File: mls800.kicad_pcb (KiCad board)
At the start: 2 copper layers, 293.4 x 80.5 mm, 106 parts, among them CON1 BARREL_JACK, IC1 6N137, J1 USB, J10 NSJ8HC, J11 NRJ4HF-1, J2 NRJ4HF-1, J3 NSJ8HC, J4 NSJ8HC, J5 NSJ8HC, J6 NSJ8HC, J7 NSJ8HC, J8 NSJ8HC, J9 NSJ8HC, P1 CONN_02X03, P2 DIN_5, P3 DIN_5, P4 CONN_02X03, P5 CONN_02X03, SW10 SW_TACT_LED, SW11 SW_TACT_LED, SW12 SW_PUSH_RIGHT_ANGLE, SW2 SW_TACT_LED, SW3 SW_TACT_LED, SW4 SW_TACT_LED, SW5 SW_TACT_LED, SW6 SW_TACT_LED, SW7 SW_TACT_LED, SW8 SW_TACT_LED, SW9 SW_TACT_LED, U1 LM340MP-5.0/NOPB, U2 ATmega32U4-AU, U3 24LC256, U4 MCP23017, U5 AS1115, U6 ULN2803A, U7 ULN2803A, U8 LM340MP-5.0/NOPB, X1 16Mhz

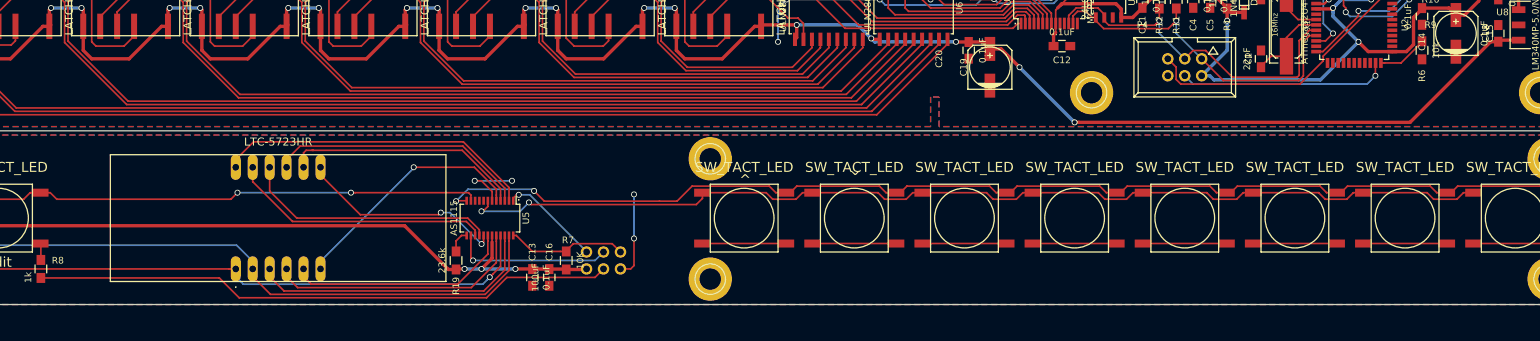
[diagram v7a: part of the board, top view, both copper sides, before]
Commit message: Fixed front panel capacitor footprint
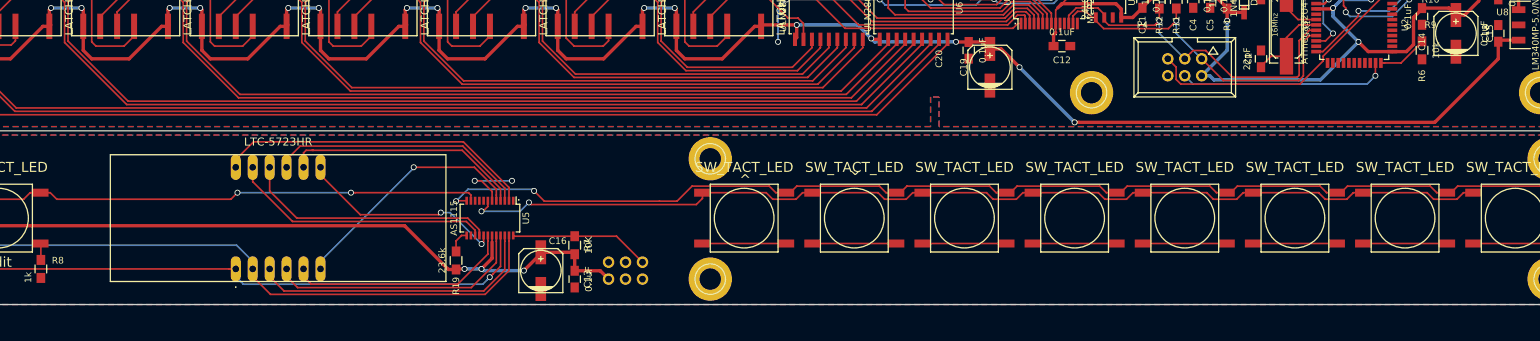
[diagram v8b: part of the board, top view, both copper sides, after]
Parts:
- C16: footprint Capacitors_SMD:C_0805_HandSoldering -> Capacitors_SMD:c_elec_6.3x7.7
- moved C13 6.36 mm to (171.4, 121.9)
- moved P5 3.64 mm to (179.1, 120.7)
- moved R7 2.62 mm to (171.4, 116.8)
- moved C16 1.63 mm to (166.4, 120.7), turned to 90 degrees
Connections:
- CON1 pad 3: (no net) -> Net-(CON1-Pad3)
- IC1 pad 7: (no net) -> Net-(IC1-Pad7)
- J11 pad 2: (no net) -> Net-(J11-Pad2)
- J2 pad 2: (no net) -> Net-(J2-Pad2)
- P2 pad 1: (no net) -> Net-(P2-Pad1)
- P2 pad 3: (no net) -> Net-(P2-Pad3)
- P2 pad 5: (no net) -> Net-(P2-Pad5)
- P3 pad 1: (no net) -> Net-(P3-Pad1)
- P3 pad 5: (no net) -> Net-(P3-Pad5)
- SW2 pad 4: /Front panel/SEGA -> /Front panel/SEGDP
- SW3 pad 4: /Front panel/SEGB -> /Front panel/SEGA
- SW4 pad 4: /Front panel/SEGC -> /Front panel/SEGB
- SW5 pad 4: /Front panel/SEGD -> /Front panel/SEGC
- SW6 pad 4: /Front panel/SEGE -> /Front panel/SEGD
- SW7 pad 4: /Front panel/SEGF -> /Front panel/SEGE
- SW8 pad 4: /Front panel/SEGG -> /Front panel/SEGF
- SW9 pad 4: /Front panel/SEGDP -> /Front panel/SEGDG
- U2 pad 12: (no net) -> Net-(U2-Pad12)
- U2 pad 21: (no net) -> Net-(U2-Pad21)
- U2 pad 24: (no net) -> Net-(U2-Pad24)
- U2 pad 25: (no net) -> Net-(U2-Pad25)
- U2 pad 26: (no net) -> Net-(U2-Pad26)
- U2 pad 27: (no net) -> Net-(U2-Pad27)
- U2 pad 28: (no net) -> Net-(U2-Pad28)
- U2 pad 29: (no net) -> Net-(U2-Pad29)
- U2 pad 30: (no net) -> Net-(U2-Pad30)
- U2 pad 31: (no net) -> Net-(U2-Pad31)
- U2 pad 36: (no net) -> Net-(U2-Pad36)
- U2 pad 37: (no net) -> Net-(U2-Pad37)
- U2 pad 38: (no net) -> Net-(U2-Pad38)
- U2 pad 39: (no net) -> Net-(U2-Pad39)
- U2 pad 40: (no net) -> Net-(U2-Pad40)
- U2 pad 41: (no net) -> Net-(U2-Pad41)
- U2 pad 42: (no net) -> Net-(U2-Pad42)
- U2 pad 44: (no net) -> Net-(U2-Pad44)
- U3 pad 7: (no net) -> Net-(U3-Pad7)
- U4 pad 19: (no net) -> Net-(U4-Pad19)
- U4 pad 20: (no net) -> Net-(U4-Pad20)
- U5 pad 10: (no net) -> Net-(U5-Pad10)
- U5 pad 8: (no net) -> Net-(U5-Pad8)
- U5 pad 9: (no net) -> Net-(U5-Pad9)
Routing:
- net /Front panel/EDIT_LED: track 87.3 -> 0.00 mm
- net /Front panel/SCL: track 24.0 -> 0.00 mm, vias 1 -> 0
- net /Front panel/SDA: track 15.2 -> 0.40 mm, vias 1 -> 0
- net /Front panel/DGND: track 31.3 -> 18.4 mm, vias 6 -> 4
- net /Front panel/SEGG: track 46.4 -> 33.9 mm
- net /Front panel/SEGDG: track 0.00 -> 12.5 mm
- net VDD: track 110.5 -> 118.3 mm
- net /Front panel/IRQ: track 18.1 -> 21.0 mm
- net +5V: track 352.9 -> 354.4 mm
